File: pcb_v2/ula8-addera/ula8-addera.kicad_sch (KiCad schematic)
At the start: 13 parts, among them J1 ula8a, U1 74LS283, U2 74LS283, U3 74LS244, U4 74LS125

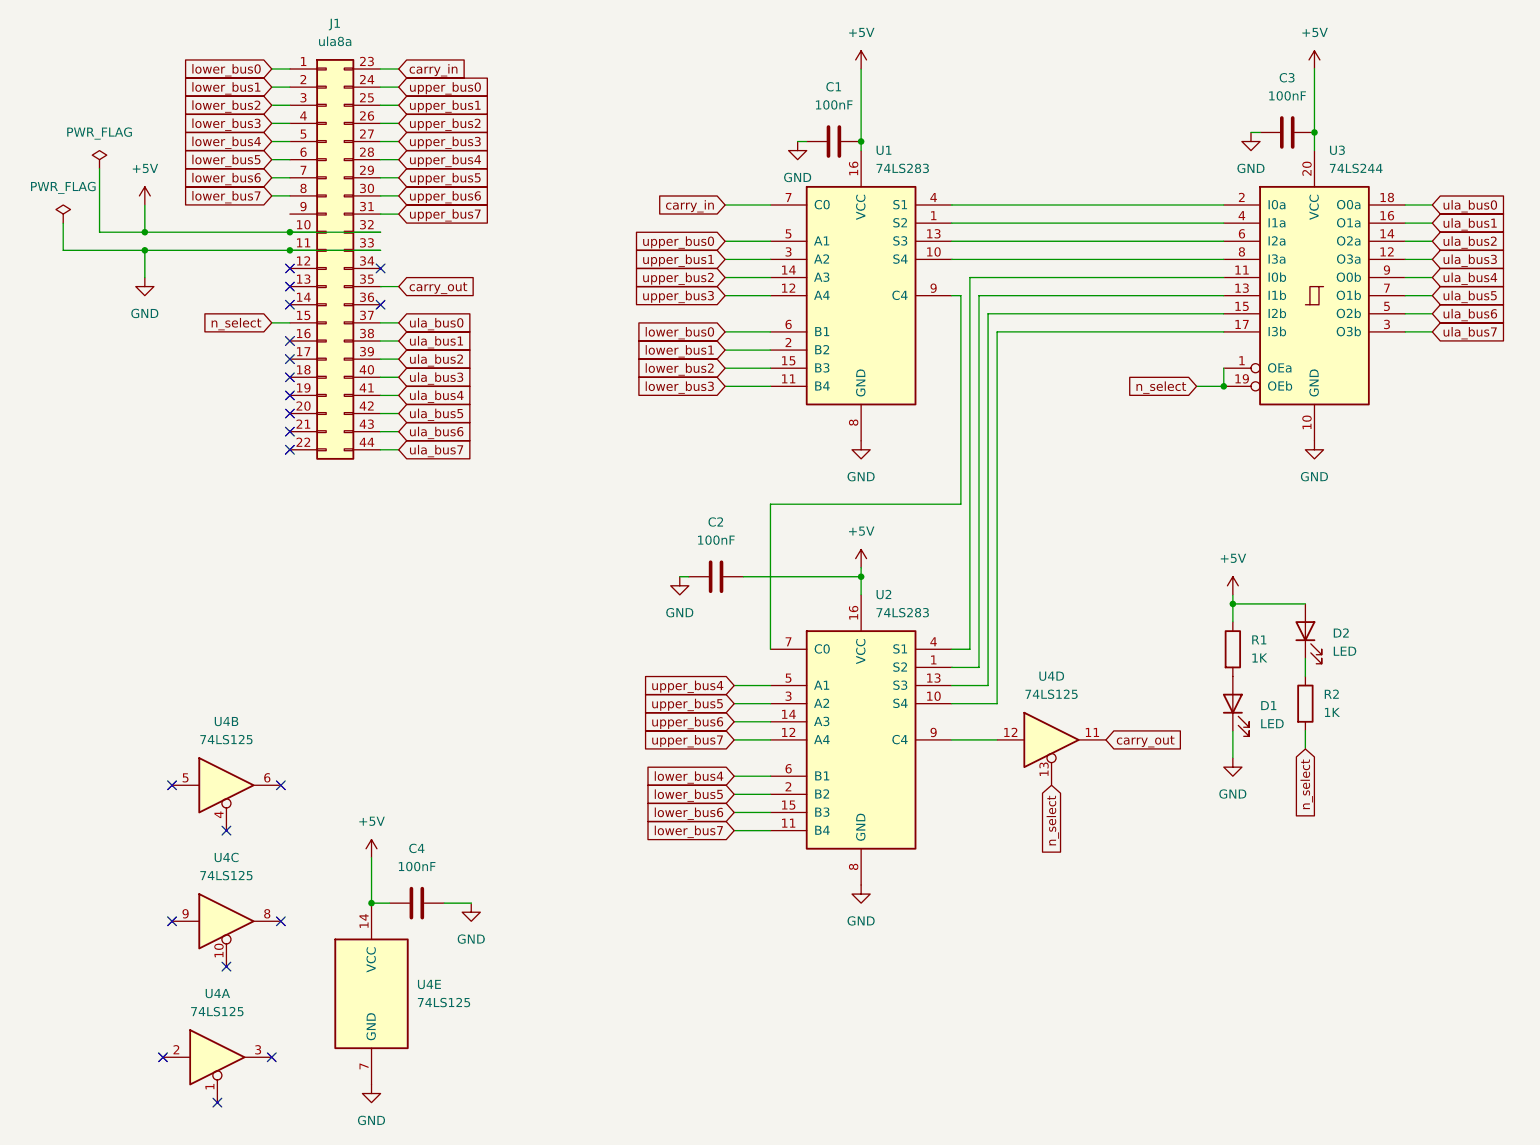
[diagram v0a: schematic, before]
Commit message: vias de alimentacao movidas para as extremidades do conector
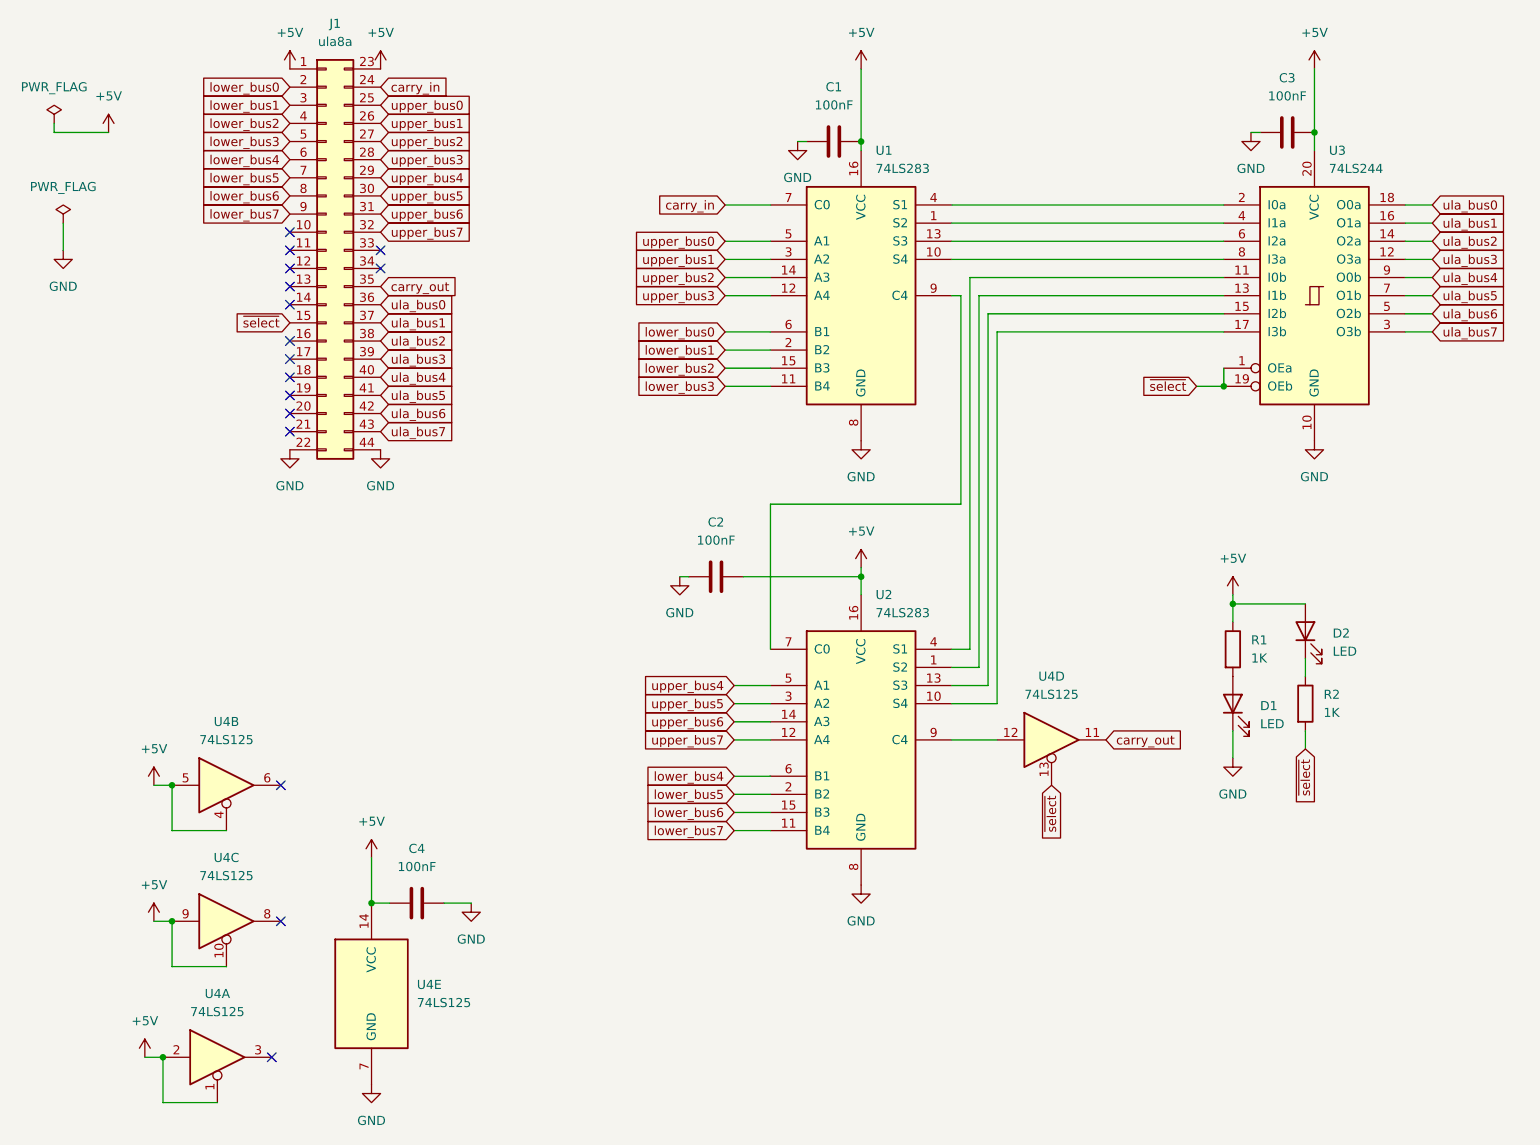
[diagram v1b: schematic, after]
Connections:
- net +5V: now also J1.1 (Pin_1), J1.23 (Pin_23), U4.1, U4.10, U4.2, U4.4, U4.5, U4.9; no longer J1.10 (Pin_10), J1.32 (Pin_32)
- net GND: now also J1.22 (Pin_22), J1.44 (Pin_44); no longer J1.11 (Pin_11), J1.33 (Pin_33)
- net carry_in: now also J1.24 (Pin_24); no longer J1.23 (Pin_23)
- net lower_bus0: now also J1.2 (Pin_2); no longer J1.1 (Pin_1)
- net lower_bus1: now also J1.3 (Pin_3); no longer J1.2 (Pin_2)
- net lower_bus2: now also J1.4 (Pin_4); no longer J1.3 (Pin_3)
- net lower_bus3: now also J1.5 (Pin_5); no longer J1.4 (Pin_4)
- net lower_bus4: now also J1.6 (Pin_6); no longer J1.5 (Pin_5)
- net lower_bus5: now also J1.7 (Pin_7); no longer J1.6 (Pin_6)
- net lower_bus6: now also J1.8 (Pin_8); no longer J1.7 (Pin_7)
- net lower_bus7: now also J1.9 (Pin_9); no longer J1.8 (Pin_8)
- net ula_bus0: now also J1.36 (Pin_36); no longer J1.37 (Pin_37)
- net ula_bus1: now also J1.37 (Pin_37); no longer J1.38 (Pin_38)
- net ula_bus2: now also J1.38 (Pin_38); no longer J1.39 (Pin_39)
- net ula_bus3: now also J1.39 (Pin_39); no longer J1.40 (Pin_40)
- net ula_bus4: now also J1.40 (Pin_40); no longer J1.41 (Pin_41)
- net ula_bus5: now also J1.41 (Pin_41); no longer J1.42 (Pin_42)
- net ula_bus6: now also J1.42 (Pin_42); no longer J1.43 (Pin_43)
- net ula_bus7: now also J1.43 (Pin_43); no longer J1.44 (Pin_44)
- net upper_bus0: now also J1.25 (Pin_25); no longer J1.24 (Pin_24)
- net upper_bus1: now also J1.26 (Pin_26); no longer J1.25 (Pin_25)
- net upper_bus2: now also J1.27 (Pin_27); no longer J1.26 (Pin_26)
- net upper_bus3: now also J1.28 (Pin_28); no longer J1.27 (Pin_27)
- net upper_bus4: now also J1.29 (Pin_29); no longer J1.28 (Pin_28)
- net upper_bus5: now also J1.30 (Pin_30); no longer J1.29 (Pin_29)
- net upper_bus6: now also J1.31 (Pin_31); no longer J1.30 (Pin_30)
- net upper_bus7: now also J1.32 (Pin_32); no longer J1.31 (Pin_31)
- net n_select renamed ~{select}
- no-connect marks 21 -> 16
